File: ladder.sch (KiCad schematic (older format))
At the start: 4 parts

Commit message: Corrected connectors.
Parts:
- C10: footprint (none) -> Capacitor_SMD:C_0603_1608Metric
- R12, R13, R14: footprint (none) -> Resistor_SMD:R_0603_1608Metric
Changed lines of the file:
@@
 F 0 "R20" H 4920 2396 50  0000 L CNN
 F 1 "1k" H 4920 2305 50  0000 L CNN
-F 2 "" V 4780 2350 50  0001 C CNN
+F 2 "Resistor_SMD:R_0603_1608Metric" V 4780 2350 50  0001 C CNN
 F 3 "~" H 4850 2350 50  0001 C CNN
 	1    4850 2350
@@
 F 0 "R21" H 4920 2796 50  0000 L CNN
 F 1 "470" H 4920 2705 50  0000 L CNN
-F 2 "" V 4780 2750 50  0001 C CNN
+F 2 "Resistor_SMD:R_0603_1608Metric" V 4780 2750 50  0001 C CNN
 F 3 "~" H 4850 2750 50  0001 C CNN
 	1    4850 2750
@@
 F 0 "R22" H 4920 3196 50  0000 L CNN
 F 1 "1k2" H 4920 3105 50  0000 L CNN
-F 2 "" V 4780 3150 50  0001 C CNN
+F 2 "Resistor_SMD:R_0603_1608Metric" V 4780 3150 50  0001 C CNN
 F 3 "~" H 4850 3150 50  0001 C CNN
 	1    4850 3150
@@
 F 0 "C13" H 5415 2996 50  0000 L CNN
 F 1 "10n" H 5415 2905 50  0000 L CNN
-F 2 "" H 5338 2800 50  0001 C CNN
+F 2 "Capacitor_SMD:C_0603_1608Metric" H 5338 2800 50  0001 C CNN
 F 3 "~" H 5300 2950 50  0001 C CNN
 	1    5300 2950

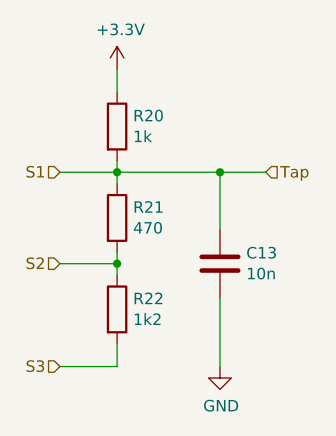
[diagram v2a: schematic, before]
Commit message: Redesigned around G431.
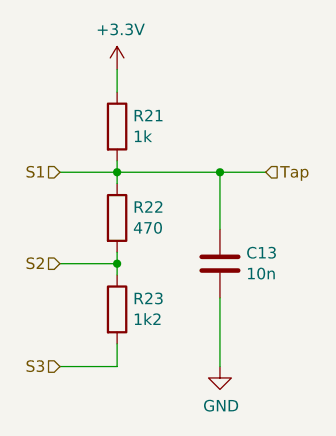
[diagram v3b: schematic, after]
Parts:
- renumbered R12 to R13, R13 to R14, R14 to R15
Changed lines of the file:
@@
 $Descr A4 11693 8268
 encoding utf-8
-Sheet 6 6
+Sheet 6 7
 Title ""
 Date ""
@@
 $EndDescr
 $Comp
-L Device:R R12
+L Device:R R13
 U 1 1 602C3C0C
 P 4850 2350
-AR Path="/602C38D4/602C3C0C" Ref="R12"  Part="1"
-AR Path="/603130AB/602C3C0C" Ref="R17"  Part="1"
-AR Path="/60321D0F/602C3C0C" Ref="R20"  Part="1"
-F 0 "R20" H 4920 2396 50  0000 L CNN
+AR Path="/602C38D4/602C3C0C" Ref="R13"  Part="1"
+AR Path="/603130AB/602C3C0C" Ref="R18"  Part="1"
+AR Path="/60321D0F/602C3C0C" Ref="R21"  Part="1"
+F 0 "R21" H 4920 2396 50  0000 L CNN
 F 1 "1k" H 4920 2305 50  0000 L CNN
 F 2 "Resistor_SMD:R_0603_1608Metric" V 4780 2350 50  0001 C CNN
@@
 $EndComp
 $Comp
-L Device:R R13
+L Device:R R14
 U 1 1 602C3CDC
 P 4850 2750
-AR Path="/602C38D4/602C3CDC" Ref="R13"  Part="1"
-AR Path="/603130AB/602C3CDC" Ref="R18"  Part="1"
-AR Path="/60321D0F/602C3CDC" Ref="R21"  Part="1"
-F 0 "R21" H 4920 2796 50  0000 L CNN
+AR Path="/602C38D4/602C3CDC" Ref="R14"  Part="1"
+AR Path="/603130AB/602C3CDC" Ref="R19"  Part="1"
+AR Path="/60321D0F/602C3CDC" Ref="R22"  Part="1"
+F 0 "R22" H 4920 2796 50  0000 L CNN
 F 1 "470" H 4920 2705 50  0000 L CNN
 F 2 "Resistor_SMD:R_0603_1608Metric" V 4780 2750 50  0001 C CNN
@@
 $EndComp
 $Comp
-L Device:R R14
+L Device:R R15
 U 1 1 602C41F1
 P 4850 3150
-AR Path="/602C38D4/602C41F1" Ref="R14"  Part="1"
-AR Path="/603130AB/602C41F1" Ref="R19"  Part="1"
-AR Path="/60321D0F/602C41F1" Ref="R22"  Part="1"
-F 0 "R22" H 4920 3196 50  0000 L CNN
+AR Path="/602C38D4/602C41F1" Ref="R15"  Part="1"
+AR Path="/603130AB/602C41F1" Ref="R20"  Part="1"
+AR Path="/60321D0F/602C41F1" Ref="R23"  Part="1"
+F 0 "R23" H 4920 3196 50  0000 L CNN
 F 1 "1k2" H 4920 3105 50  0000 L CNN
 F 2 "Resistor_SMD:R_0603_1608Metric" V 4780 3150 50  0001 C CNN
